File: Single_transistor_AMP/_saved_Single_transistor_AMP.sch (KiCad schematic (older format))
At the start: 11 parts, among them P1 Input, P2 output, P3 power, Q1 BC548

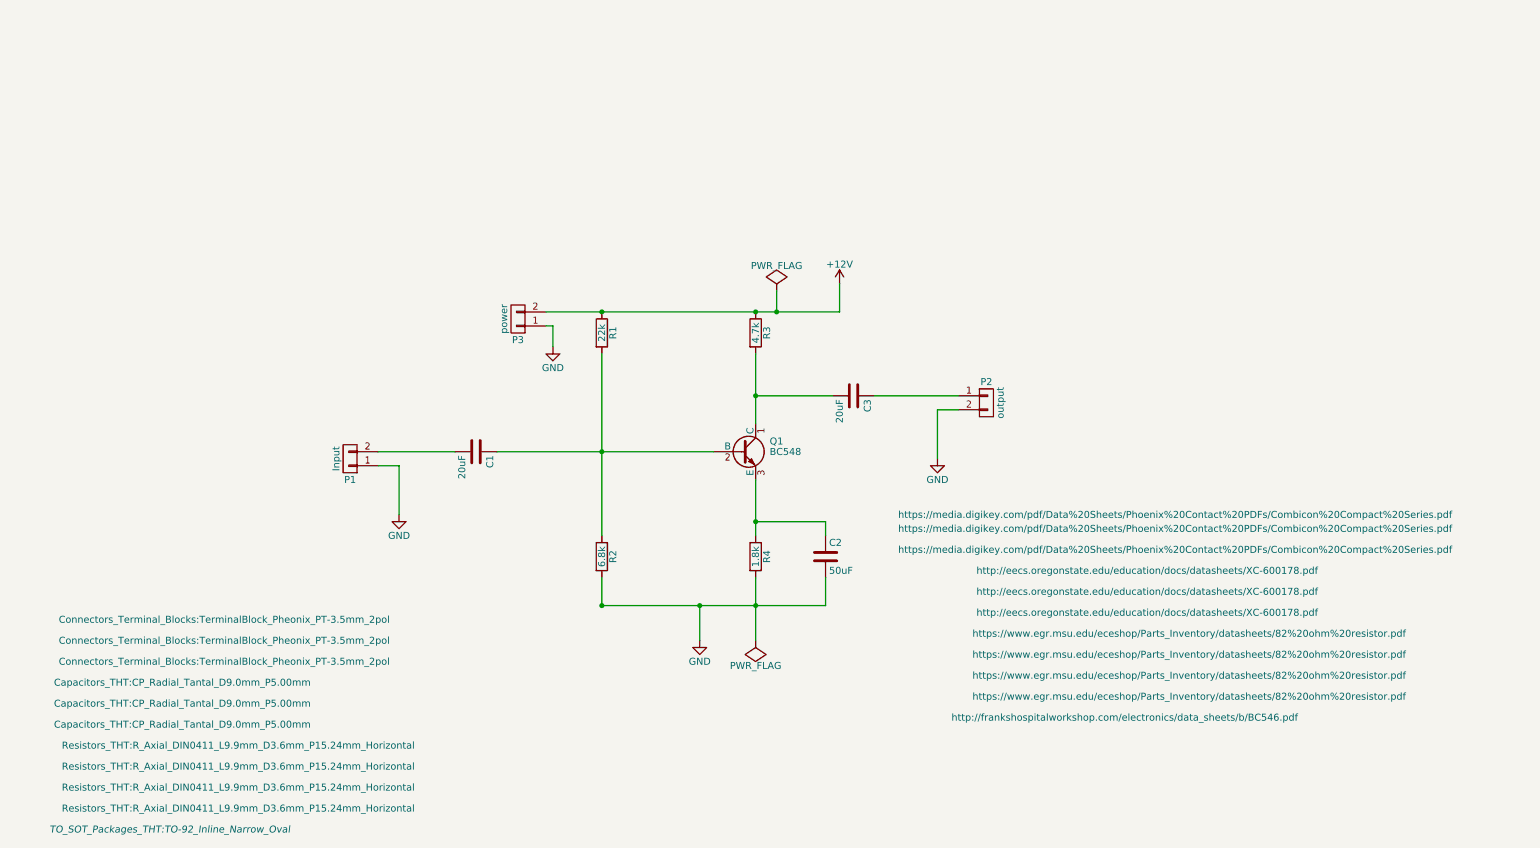
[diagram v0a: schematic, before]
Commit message: Single transistor amp pabeigs komponensu layout
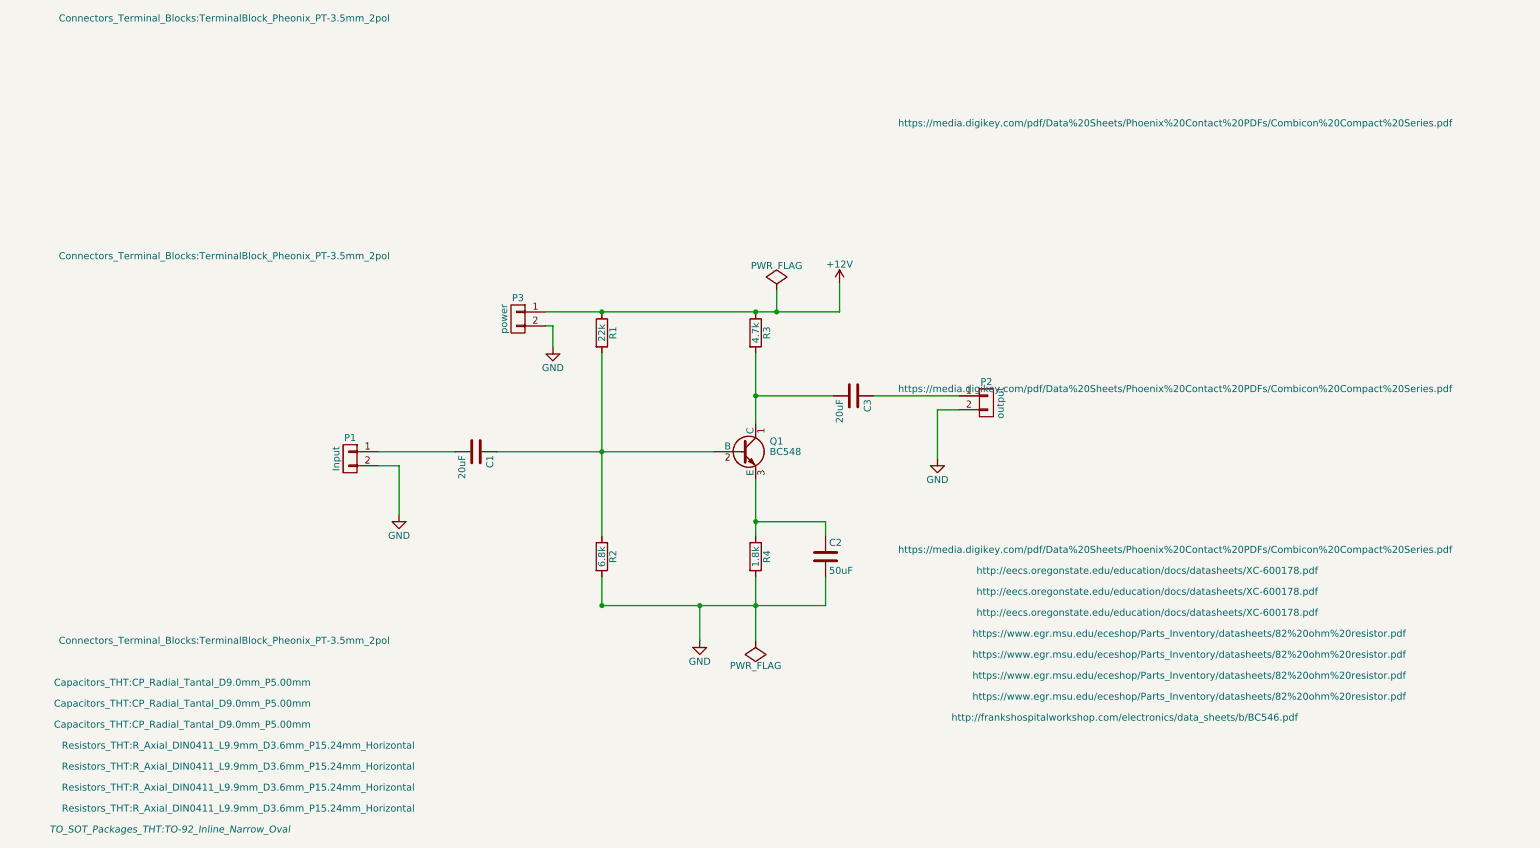
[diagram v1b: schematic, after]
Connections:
- net +12V: now also P3.1 (P1); no longer P3.2 (P2)
- net GND: now also P1.2 (P2), P3.2 (P2); no longer P1.1 (P1), P3.1 (P1)
- net at C1.2: now also P1.1 (P1); no longer P1.2 (P2)
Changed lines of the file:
@@
 F 3 "https://media.digikey.com/pdf/Data%20Sheets/Phoenix%20Contact%20PDFs/Combicon%20Compact%20Series.pdf" H -2650 4350 50  0000 C CNN
 	1    3250 3850
-	-1   0    0    1
+	-1   0    0    -1
 $EndComp
 $Comp
@@
 F 3 "https://media.digikey.com/pdf/Data%20Sheets/Phoenix%20Contact%20PDFs/Combicon%20Compact%20Series.pdf" H -250 4250 50  0000 C CNN
 	1    4450 2850
-	-1   0    0    1
+	-1   0    0    -1
 $EndComp
 Connection ~ 5050 2800
